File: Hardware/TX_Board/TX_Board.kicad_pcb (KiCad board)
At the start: 4 copper layers, 148.3 x 98.8 mm, 224 parts, among them IC1 GP2Y1+, IC10 QPA9122TR7, IC11 MAPS-010164-TR0500, IC12 QPA9122TR7, IC13 MAPS-010164-TR0500, IC14 QPA9122TR7, IC2 GP2Y1+, IC3 GP2Y1+, IC4 LT3041ADE#PBF, IC5 LT3099ADE#PBF, IC6 ADPL40502AUJZ-1.5-R7, IC7 MAPS-010164-TR0500, IC8 QPA9122TR7, IC9 MAPS-010164-TR0500, J1 Conn_Coaxial, J10 MM8030-2610RJ3, J11 MM8030-2610RJ3, J12 MM8030-2610RJ3, J13 MM8030-2610RJ3, J14 MM8030-2610RJ3, J15 Conn_Coaxial, J16 MM8030-2610RJ3, J17 MM8030-2610RJ3, J18 Conn_Coaxial, J19 MM8030-2610RJ3, J2 Conn_01x01_Pin, J20 MM8030-2610RJ3, J21 Conn_Coaxial, J22 MM8030-2610RJ3, J23 MM8030-2610RJ3, J24 Conn_Coaxial, J3 Conn_01x01_Pin, J4 Conn_01x01_Pin, J5 Conn_01x01_Pin, J6 Conn_02x12_Odd_Even, J7 Conn_01x03_Socket, J8 Conn_02x08_Odd_Even, J9 MM8030-2610RJ3, U1 SN74HCT138NSR

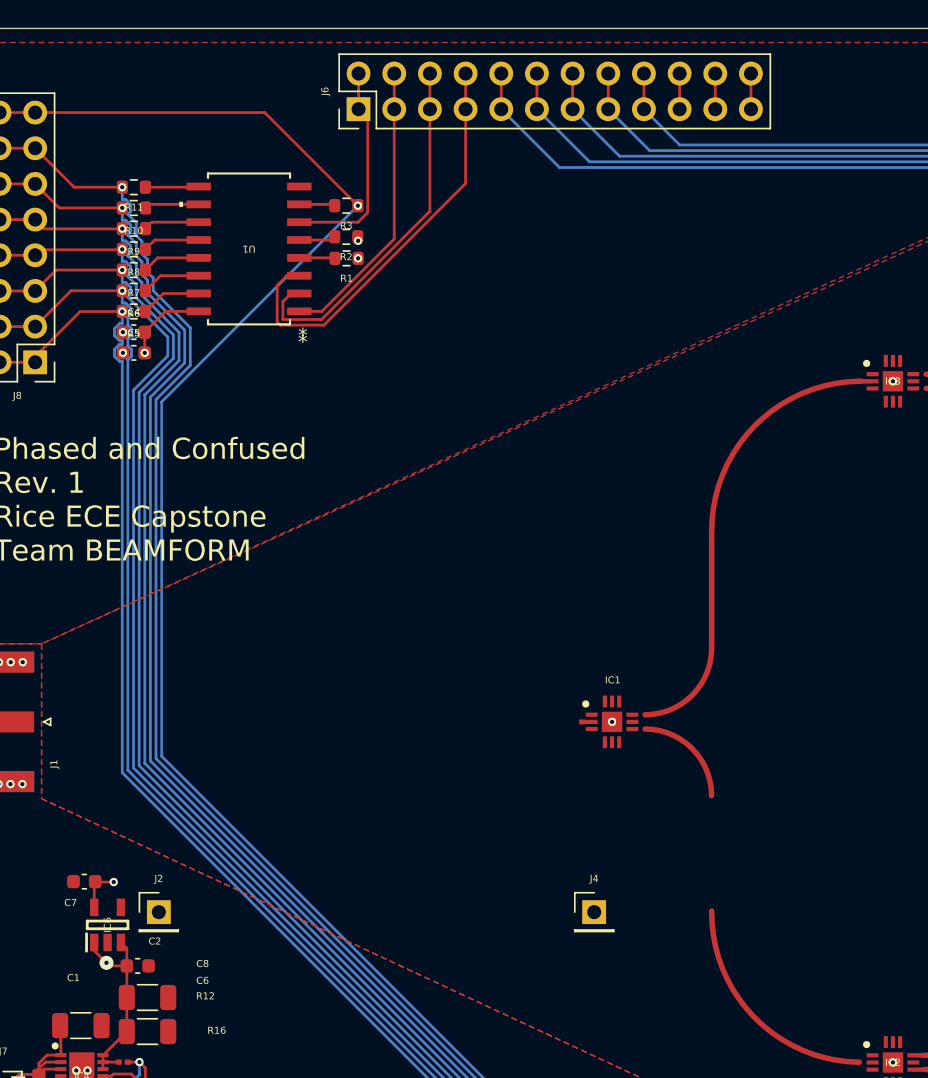
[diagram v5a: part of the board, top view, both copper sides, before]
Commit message: added power breakout pins.
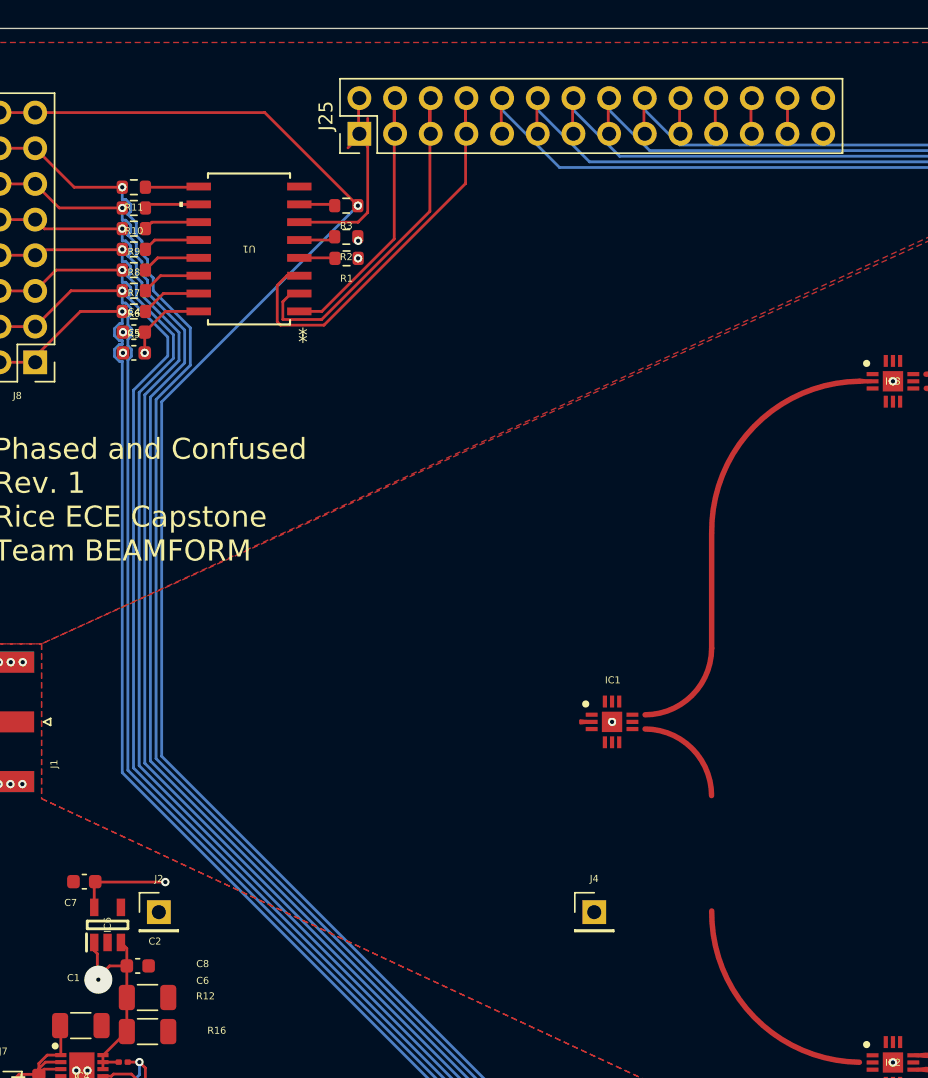
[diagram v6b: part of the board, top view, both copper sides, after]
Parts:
- removed J6: Conn_02x12_Odd_Even, Connector_PinHeader_2.54mm:PinHeader_2x12_P2.54mm_Vertical
- added J25: Conn_02x14_Odd_Even, Connector_PinHeader_2.54mm:PinHeader_2x14_P2.54mm_Vertical, F.Cu at (110.6, 37.5)
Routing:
- net V_PD: track 223.7 -> 292.1 mm
- net VEE: track 223.7 -> 263.1 mm
- net GND: track 219.5 -> 214.4 mm
- net VCC: track 125.5 -> 130.0 mm
